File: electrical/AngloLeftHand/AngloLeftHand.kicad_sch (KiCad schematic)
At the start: 49 parts, among them J3 TC2030-NL, U1 DRV5053VAQDBZR, U10 DRV5053VAQDBZR, U11 DRV5053VAQDBZR, U12 DRV5053VAQDBZR, U13 DRV5053VAQDBZR, U14 DRV5053VAQDBZR, U15 DRV5053VAQDBZR, U16 STM32L072CBTx, U17 CD74HC4067SM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

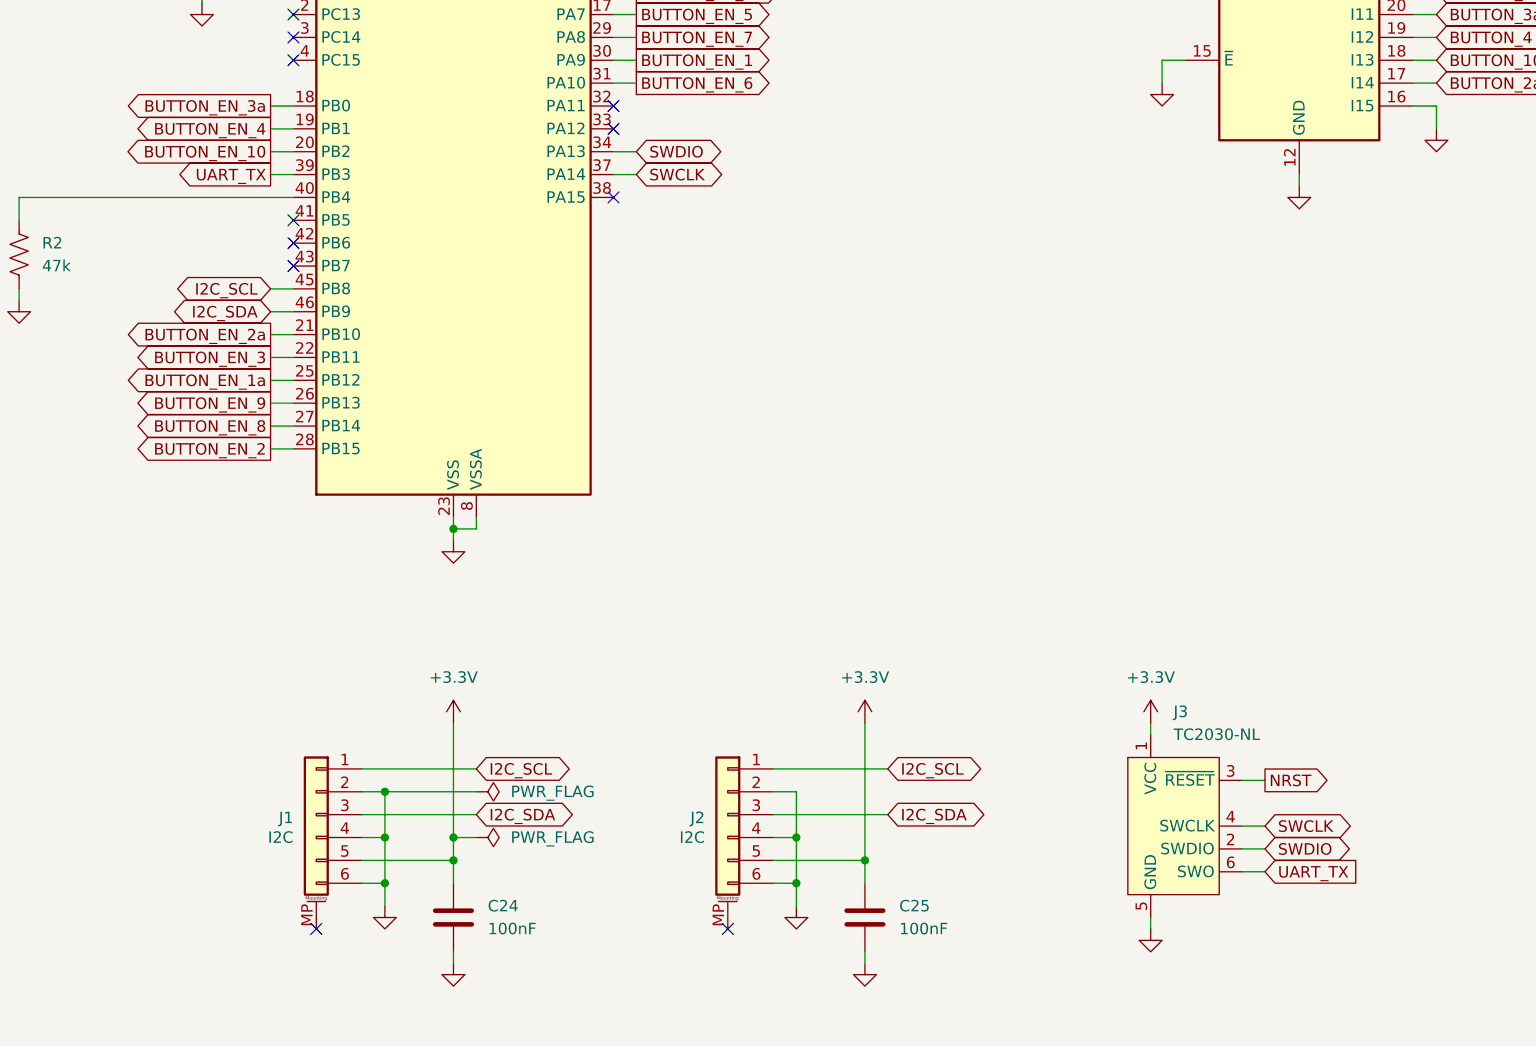
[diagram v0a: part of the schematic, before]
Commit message: Remove UART from debug connector
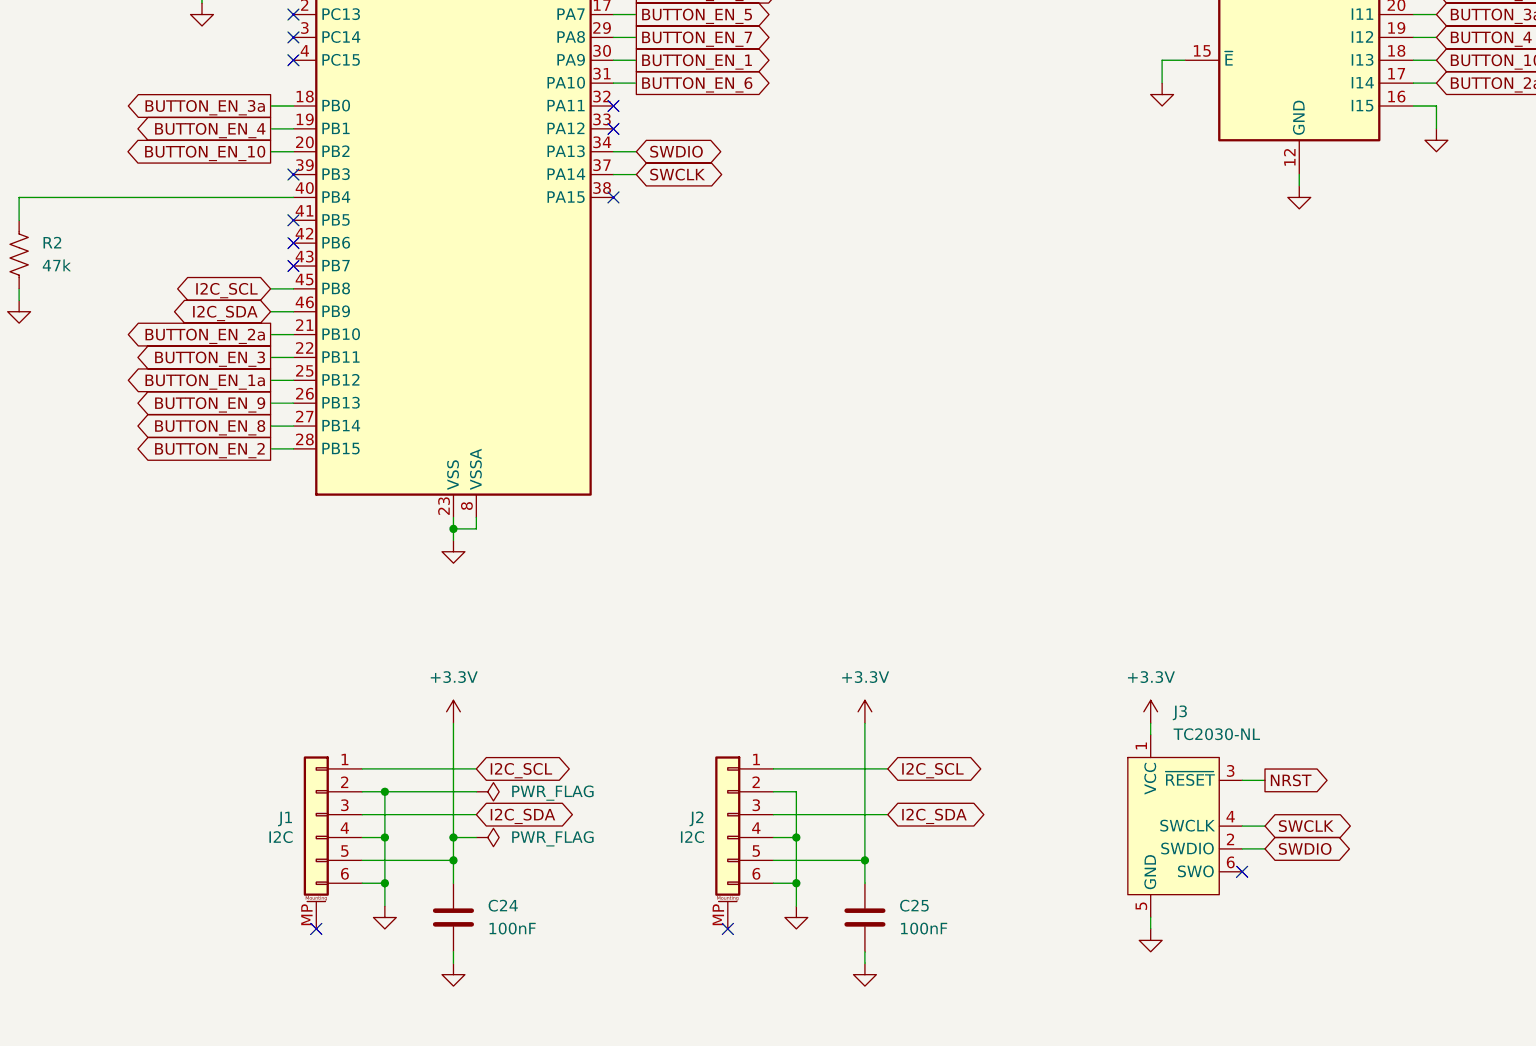
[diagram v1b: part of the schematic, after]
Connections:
- net UART_TX: no longer names the net of U16.39 (PB3)
- net UART_TX: no longer J3.6 (SWO)
- no-connect marks 13 -> 15
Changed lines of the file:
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@@
 	)
 	(no_connect
+		(at 88.9 110.49)
+	)
+	(no_connect
 		(at 88.9 85.09)
 	)
@@
 	)
 	(no_connect
+		(at 194.31 187.96)
+	)
+	(no_connect
 		(at 88.9 120.65)
 	)
@@
 	(wire
 		(pts
-			(xy 196.85 187.96) (xy 194.31 187.96)
-		)
-		(stroke
-			(width 0)
-			(type default)
-		)
-	)
-	(wire
-		(pts
 			(xy 335.28 149.86) (xy 337.82 149.86)
 		)
@@
 	(wire
 		(pts
-			(xy 86.36 110.49) (xy 88.9 110.49)
-		)
-		(stroke
-			(width 0)
-			(type default)
-		)
-	)
-	(wire
-		(pts
 			(xy 215.9 77.47) (xy 213.36 77.47)
 		)
@@
 		)
 	)
-	(global_label "UART_TX"
-		(shape output)
-		(at 86.36 110.49 180)
-		(fields_autoplaced yes)
-		(effects
-			(font
-				(size 1.27 1.27)
-			)
-			(justify right)
-		)
-		(property "Intersheetrefs" "${INTERSHEET_REFS}"
-			(at 75.5734 110.49 0)
-			(effects
-				(font
-					(size 1.27 1.27)
-				)
-				(justify right)
-				(hide yes)
-			)
-		)
-	)
 	(global_label "BUTTON_EN_5a"
 		(shape output)
@@
 				(hide yes)
 			)
-		)
-	)
-	(global_label "UART_TX"
-		(shape input)
-		(at 196.85 187.96 0)
-		(fields_autoplaced yes)
-		(effects
-			(font
-				(size 1.27 1.27)
-			)
-			(justify left)
-		)
-		(property "Intersheetrefs" "${INTERSHEET_REFS}"
-			(at 207.6366 187.96 0)
-			(effects
-				(font
-					(size 1.27 1.27)
-				)
-				(justify left)
-				(hide yes)
-			)

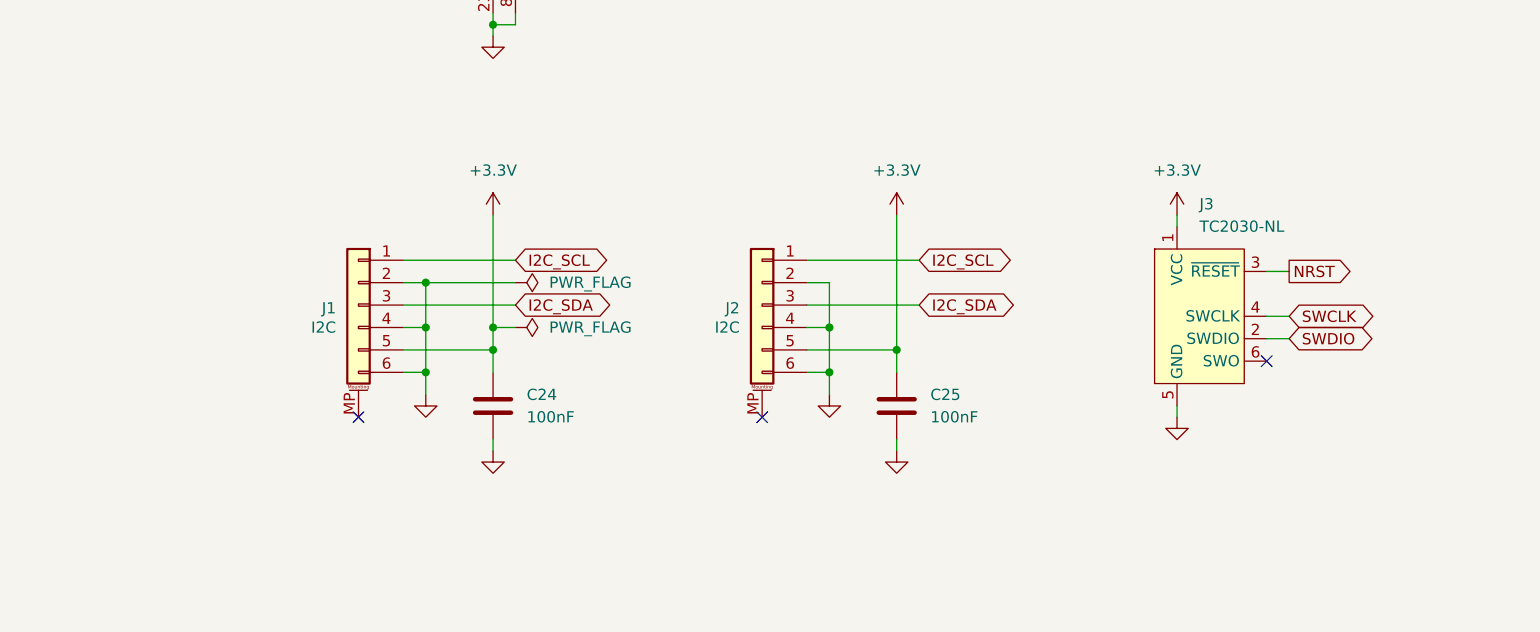
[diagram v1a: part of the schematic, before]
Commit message: Replace PicoBlade connectors with SKEDD
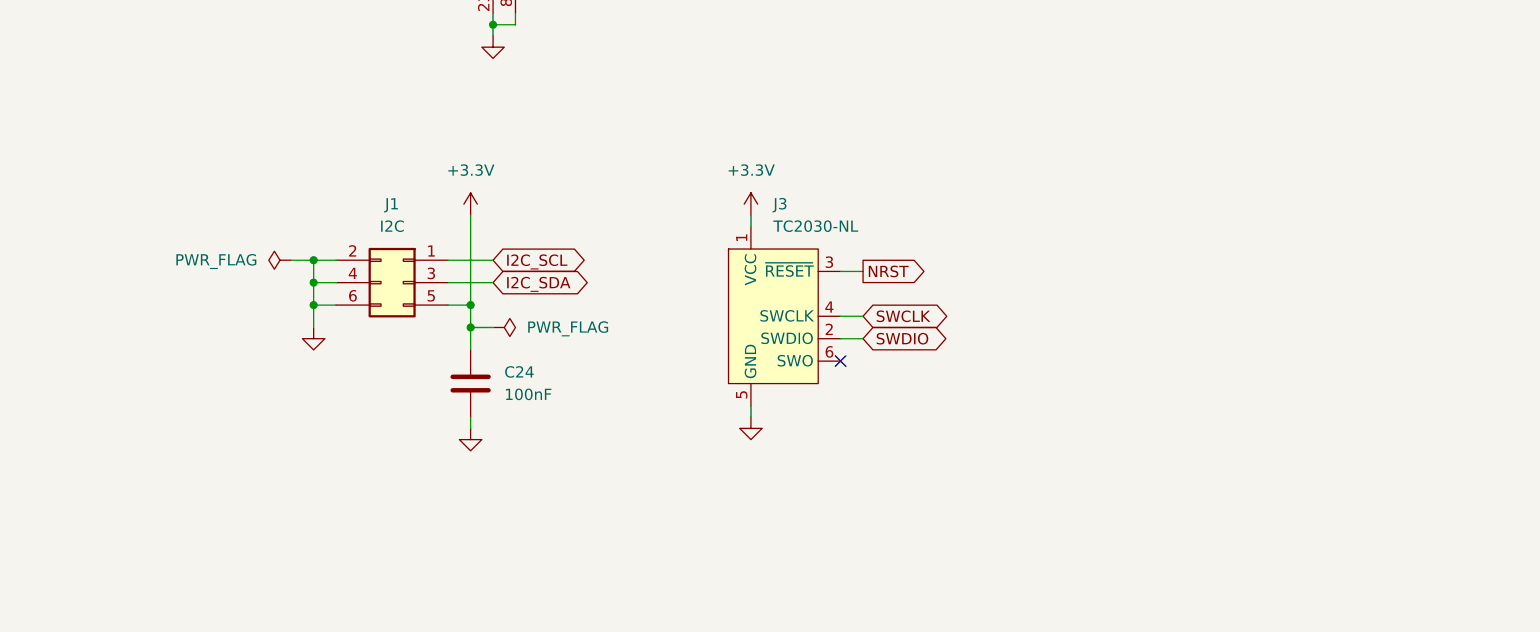
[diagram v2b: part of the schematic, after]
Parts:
- removed C25: 100nF, Capacitor_SMD:C_0402_1005Metric, symbol Device:C
- removed J1, J2: ~, Connector_Molex:Molex_PicoBlade_53261-0671_1x06-1MP_P1.25mm_Horizontal, symbol Connector_Generic_MountingPin:Conn_01x06_MountingPin
- added J1: I2C, MidiConcertina:Wuerth_WR-WST_490107670612_2x03_P2.54mm_SKEDD, symbol Connector_Generic:Conn_02x03_Odd_Even
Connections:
- net +3.3V: now also J1.5 (Pin_5)
- net GND: now also J1.2 (Pin_2), J1.4 (Pin_4), J1.6 (Pin_6)
- net I2C_SCL: now also J1.1 (Pin_1)
- net I2C_SDA: now also J1.3 (Pin_3)
- no-connect marks 15 -> 13
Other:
- moved on the sheet: C24, J3

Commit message: Relabel components
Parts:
- renumbered J3 to J2
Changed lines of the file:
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@@
 		(on_board yes)
 		(dnp no)
-		(property "Reference" "J3"
+		(property "Reference" "J2"
 			(at 138.43 170.18 0)
 			(effects
@@
 			(project "control"
 				(path "/da26d94e-7a50-4b99-9678-5aaaf6987a15"
-					(reference "J3")
+					(reference "J2")
 					(unit 1)
 				)
